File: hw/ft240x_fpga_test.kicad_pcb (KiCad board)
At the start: 4 copper layers, 100 x 42.4 mm, 224 parts, among them J1 Ext_Power, J11 PEN_SEL, J2 USB_C_Receptacle_USB2.0, J3 Jtag_Master, J4 JTAG, J5 GPIO2V5, J6 BNC, J7 BNC, J8 BNC, J9 Conn_02x04_Odd_Even, Q1 Si3477, U1 TLV62569DDC, U10 LMH6882, U11 TSV992A, U12 OPA859xDSG, U13 OPA859xDSG, U14 MCP47CVB02-E_UN, U15 UTC2000, U16 74LVC1G32, U2 TLV62569DDC, U3 TLV62569DDC, U4 FT240XS, U5 XC3S50A-VQ100, U6 AT25DF041B, U7 5P49V5925, U8 THS4522, U9 MAX19507, Y1 25MHz

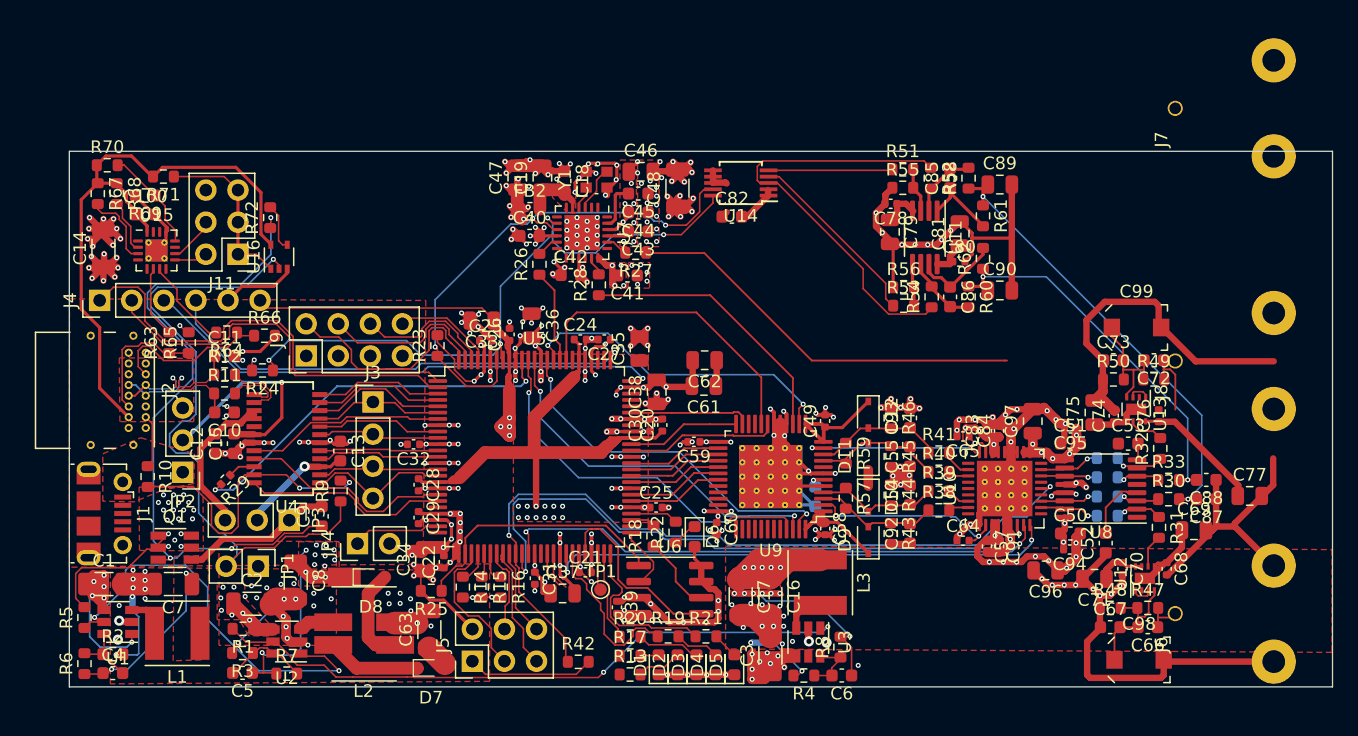
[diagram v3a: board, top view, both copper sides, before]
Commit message: everything hooked up + layed out; 0.2/0.4mm vias :-(
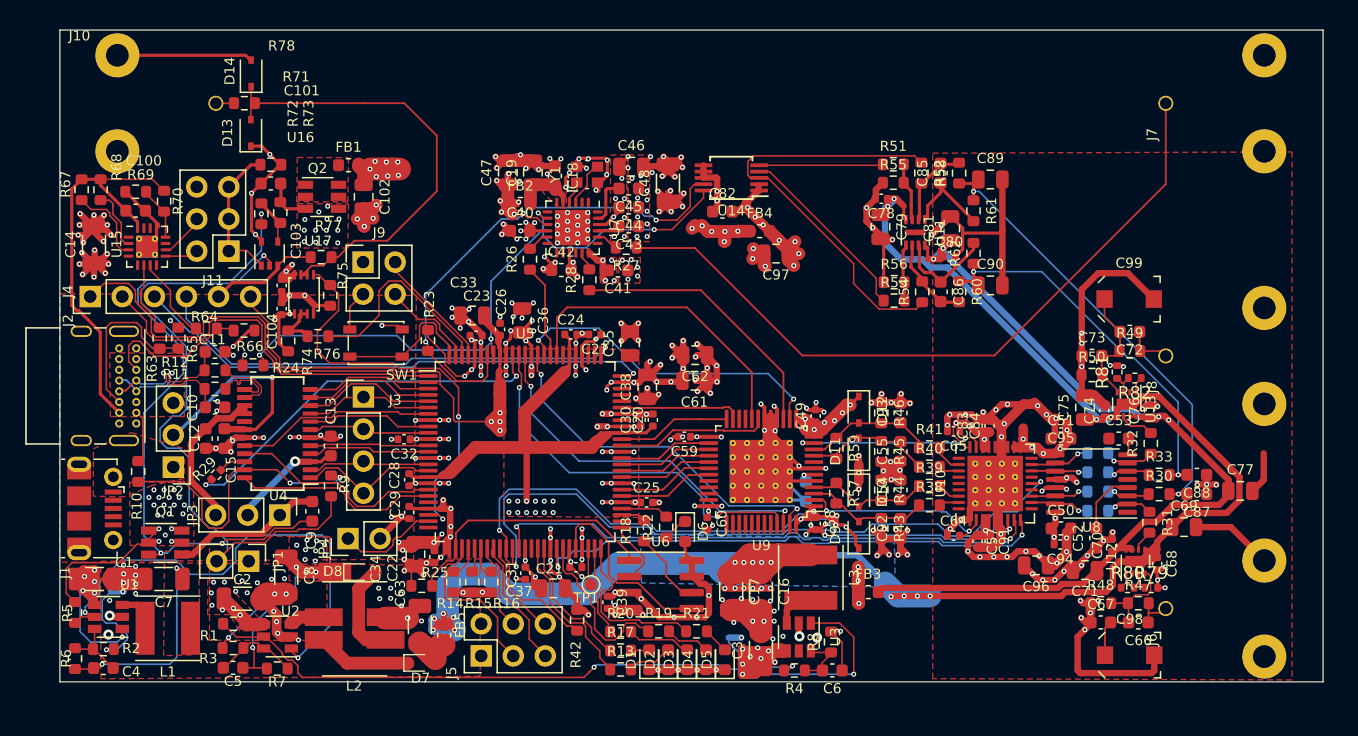
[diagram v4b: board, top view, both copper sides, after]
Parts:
- added C101: 100n, Capacitor_SMD:C_0603_1608Metric, F.Cu at (79.7, 39.4)
- added C102: 1u, Capacitor_SMD:C_0805_2012Metric, F.Cu at (87.0, 40.4)
- added C103: 100n, Capacitor_SMD:C_0402_1005Metric, F.Cu at (80.6, 47.4)
- added C104: 100n, Capacitor_SMD:C_0402_1005Metric, F.Cu at (80.6, 49.3)
- added D13: NSR0170HT1G, Diode_SMD:D_SOD-323, F.Cu at (78.1, 35.3)
- added D14: NSR0170HT1G, Diode_SMD:D_SOD-323, F.Cu at (78.1, 30.6)
- added FB1: Ferrite_Bead MPZ1608S221A, Inductor_SMD:L_0603_1608Metric, F.Cu at (85.8, 37.9)
- added FB3: Ferrite_Bead MPZ1608S221A, Inductor_SMD:L_0603_1608Metric, F.Cu at (127.0, 71.7)
- added FB4: Ferrite_Bead MPZ1608S221A, Inductor_SMD:L_0603_1608Metric, F.Cu at (118.4, 43.1)
- added FB5: Ferrite_Bead MPZ1608S221A, Inductor_SMD:L_0603_1608Metric, F.Cu at (93.4, 75.1)
- added J10: BNC, proj_footprints:BNC_Molex_0731713150, F.Cu at (67.5, 33.0)
- added Q2: Si3477, Package_TO_SOT_SMD:TSOT-23-6, F.Cu at (83.8, 40.4)
- added R73: 100k, Resistor_SMD:R_0603_1608Metric, F.Cu at (80.5, 41.6)
- added R74: 100k, Resistor_SMD:R_0603_1608Metric, F.Cu at (81.1, 51.8)
- added R75: 2k2, Resistor_SMD:R_0603_1608Metric, F.Cu at (84.4, 48.2)
- added R76: 100, Resistor_SMD:R_0603_1608Metric, F.Cu at (83.4, 51.4)
- added R77: 100k, Resistor_SMD:R_0603_1608Metric, F.Cu at (83.7, 45.2)
- added R78: 50, Resistor_SMD:R_0603_1608Metric, F.Cu at (77.6, 33.0)
- added R79: 750, Resistor_SMD:R_0402_1005Metric, F.Cu at (149.4, 71.3)
- added R80: 750, Resistor_SMD:R_0402_1005Metric, F.Cu at (147.5, 71.3)
- added R81: 750, Resistor_SMD:R_0402_1005Metric, F.Cu at (146.7, 54.3)
- added R82: 750, Resistor_SMD:R_0402_1005Metric, F.Cu at (148.1, 54.8)
- added SW1: PROG_B, Button_Switch_SMD:SW_SPST_PTS810, F.Cu at (88.0, 52.0)
- added U17: SN74LVC2T45DCUR, Package_SO:VSSOP-8_2.4x2.1mm_P0.5mm, F.Cu at (82.3, 48.1)
- C67, C73: value 10p -> 15p
- J9: value Conn_02x04_Odd_Even -> PUDC/IN; footprint Connector_PinHeader_2.54mm:PinHeader_2x04_P2.54mm_Vertical -> Connector_PinHeader_2.54mm:PinHeader_2x02_P2.54mm_Vertical
- R38, R39, R40, R41: value 176 -> 178
- U11: footprint Package_SO:MSOP-8_3x3mm_P0.65mm -> proj_footprints:DFN-8-1EP_2x2mm_P0.5mm_EP0.45x1.6mm
- moved C97 24.3 mm to (119.7, 44.9), turned to 180 degrees
- moved J9 8.69 mm to (87.0, 45.6), turned to 0 degrees
- moved R71 8.55 mm to (79.7, 37.9), turned to 0 degrees
- moved R70 5.33 mm to (71.2, 40.8), turned to 270 degrees
- moved R42 3.29 mm to (104.0, 73.9), turned to 90 degrees
- moved C72 2.94 mm to (147.7, 51.1)
- moved R49 2.94 mm to (147.7, 52.6)
- moved C99 2.32 mm to (147.7, 48.5)
- moved C70 2.02 mm to (146.3, 68.0), turned to 90 degrees
- moved NT3 1.84 mm to (116.5, 75.3), turned to 0 degrees
- moved C73 1.74 mm to (144.7, 53.0)
- moved R50 1.74 mm to (144.7, 54.5)
- moved R66 1.67 mm to (77.6, 51.0)
- moved R64 1.63 mm to (74.6, 50.8)
- moved U12 1.53 mm to (148.1, 69.3)
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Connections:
- net Net-(J7-Pad1) renamed /pll_clock/CLK_OUT
- net Net-(R72-Pad2) renamed /Power/PWR_EN
- C49 pad 2: GNDA -> GND
- C50 pad 1: GNDA -> GND
- C51 pad 1: GNDA -> GND
- C52 pad 1: GNDA -> GND
- C53 pad 1: GNDA -> GND
- C57 pad 2: GNDA -> GND
- C58 pad 2: GNDA -> GND
- C63 pad 1: -2V5 -> Net-(C63-Pad1)
- C64 pad 1: GNDA -> GND
- C65 pad 2: GNDA -> GND
- C67 pad 1: GNDA -> GND
- C68 pad 2: GNDA -> GND
- C69 pad 2: GNDA -> GND
- C70 pad 2: GNDA -> GND
- C71 pad 2: GNDA -> GND
- C73 pad 1: GNDA -> GND
- C74 pad 2: GNDA -> GND
- C75 pad 2: GNDA -> GND
- C76 pad 2: GNDA -> GND
- C77 pad 2: GNDA -> GND
- C78 pad 2: GNDA -> GND
- C79 pad 2: GNDA -> GND
- C80 pad 2: GNDA -> GND
- C81 pad 2: GNDA -> GND
- C82 pad 1: GNDA -> GND
- C83 pad 2: GNDA -> GND
- C84 pad 2: GNDA -> GND
- C87 pad 1: GNDA -> GND
- C88 pad 1: GNDA -> GND
- C89 pad 2: GNDA -> GND
- C90 pad 2: GNDA -> GND
- C91 pad 2: GNDA -> GND
- C94 pad 2: GNDA -> GND
- C95 pad 2: GNDA -> GND
- C96 pad 2: GNDA -> GND
- C97 pad 1: Vpp_analog -> +1V8_analog
- C97 pad 2: GNDA -> GND
- C98 pad 2: GNDA -> GND
- C99 pad 2: GNDA -> GND
- D7 pad 2: -2V5 -> Net-(C63-Pad1)
- J6 pad 2: GNDA -> GND
- J8 pad 2: GNDA -> GND
- R48 pad 1: GNDA -> GND
- R50 pad 1: GNDA -> GND
- R55 pad 1: GNDA -> GND
- R56 pad 1: GNDA -> GND
- R71 pad 2: VBUS -> +5V
- U10 pad 1: GNDA -> GND
- U10 pad 21: GNDA -> GND
- U10 pad 22: GNDA -> GND
- U10 pad 23: GNDA -> GND
- U10 pad 37: GNDA -> GND
- U10 pad 5: GNDA -> GND
- U10 pad 6: GNDA -> GND
- U12 pad 1: Net-(U12-Pad1) -> Net-(R80-Pad1)
- U12 pad 3: Net-(U12-Pad1) -> Net-(R79-Pad1)
- U13 pad 1: Net-(U13-Pad1) -> Net-(R82-Pad1)
- U13 pad 3: Net-(U13-Pad1) -> Net-(R81-Pad1)
- U14 pad 6: GNDA -> GND
- U14 pad 7: GNDA -> GND
- U14 pad 8: GNDA -> GND
- U16 pad 5: VBUS -> +5V
- U5 pad 100: Net-(J9-Pad2) -> Net-(SW1-Pad1)
- U5 pad 23: GND -> /fpga_xc3s/IO_DIR
- U5 pad 97: Net-(J9-Pad8) -> Net-(J9-Pad2)
- U5 pad 98: Net-(J9-Pad6) -> /fpga_xc3s/IO_DAT
- U8 pad 12: GNDA -> GND
- U8 pad 16: GNDA -> GND
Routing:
- net GND: track 236.2 -> 419.1 mm, vias 225 -> 304
- net GNDA: track 161.6 -> 0.00 mm, vias 40 -> 0
- net -2V5: track 16.6 -> 156.3 mm, vias 0 -> 13
- net +2V5_analog: track 17.6 -> 75.4 mm, vias 0 -> 4
- net Net-(D13-Pad2): track 0.00 -> 36.6 mm
- net /fpga_xc3s/IO_DIR: track 0.00 -> 33.0 mm, vias 0 -> 2
- net /pll_clock/CLK_OUT: track 31.9 -> 57.2 mm
- net +2V5: track 100.7 -> 125.6 mm, vias 38 -> 39
- net +1V8_analog: track 23.6 -> 44.5 mm, vias 0 -> 22
- net +1V8: track 83.7 -> 103.1 mm, vias 76 -> 92
- net /fpga_xc3s/IO_DAT: track 0.00 -> 16.6 mm
- net VBUS: track 52.4 -> 37.1 mm
- net +5V: track 81.3 -> 95.5 mm, vias 32 -> 49
- net Net-(SW1-Pad1): track 0.00 -> 11.6 mm
- net Net-(J9-Pad6): track 11.2 -> 0.00 mm
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- added copper zone on In2.Cu, net +1V8_analog
- added copper zone on B.Cu, net -2V5
- added copper zone on F.Cu, net Net-(FB1-Pad1)
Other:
- board size 100 x 42.4 mm -> 100 x 51.6 mm
- net class 50OhmLine added: clearance 0.5, trace_width 0.147, via_dia 0.4, via_drill 0.2

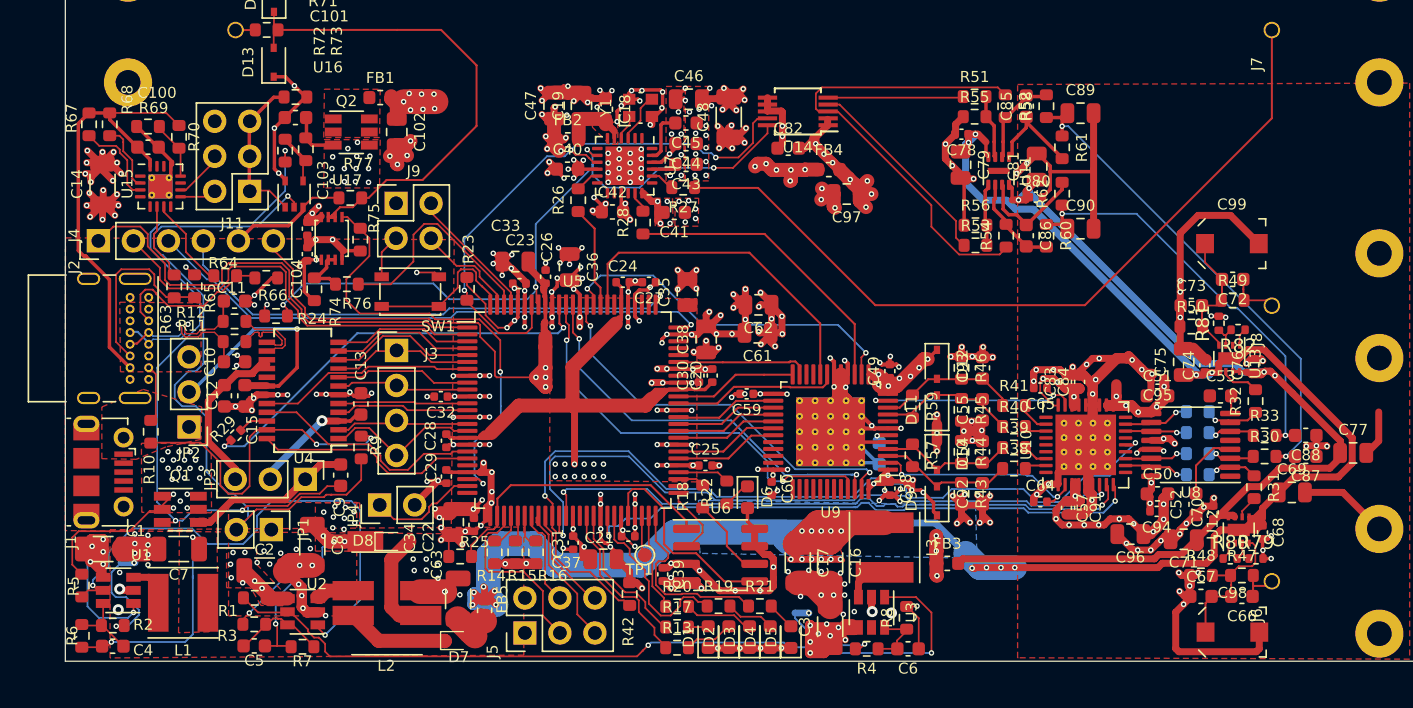
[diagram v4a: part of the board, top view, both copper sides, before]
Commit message: pcb: increased min. via dia to 0.45mm (jlcpcb)
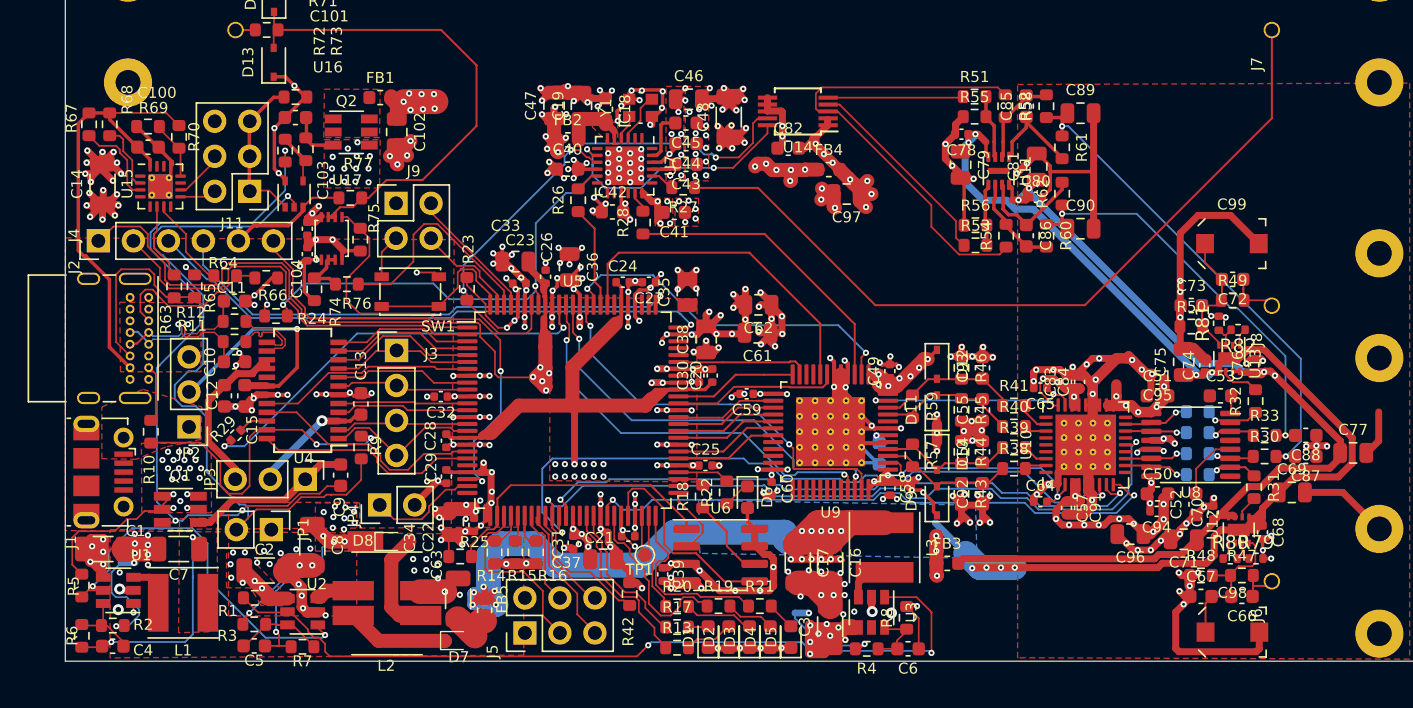
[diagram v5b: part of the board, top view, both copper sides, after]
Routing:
- net -2V5: track 156.3 -> 136.2 mm
- net Net-(R5-Pad1): track 39.3 -> 28.7 mm
- net +5V: track 95.5 -> 88.4 mm
- net GND: track 419.1 -> 422.0 mm, vias 304 -> 307
- net +1V2: track 83.3 -> 85.9 mm, vias 26 -> 27
- net PGA_SDO: track 64.0 -> 61.5 mm
- net +1V8: track 103.1 -> 105.0 mm, vias 92 -> 94
- net PGA_SCLK: track 44.0 -> 45.6 mm
- net +1V8_analog: track 44.5 -> 43.1 mm
- net PGA_CSb: track 41.7 -> 42.9 mm
- net PGA_SDI: track 50.4 -> 51.3 mm
- net Net-(C64-Pad2): track 15.8 -> 16.7 mm
- net ADC_SDIO: track 30.8 -> 30.1 mm
- net +2V5: track 125.6 -> 126.1 mm, vias 39 -> 40
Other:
- net class 50OhmLine: via_dia 0.4 -> 0.45
- net class Default: via_dia 0.4 -> 0.45
- net class clr3p5: via_dia 0.4 -> 0.45
- rule via_min_size: 0.4 -> 0.45

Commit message: prototype version
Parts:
- added D15: LED_Front, proj_footprints:LED_Wuerth_Sideview, F.Cu at (65.6, 41.5)
- added J12: PUDC_B/IN, Connector_PinHeader_2.54mm:PinHeader_2x02_P2.54mm_Vertical, F.Cu at (89.5, 48.3)
- added R83: 1k5, Resistor_SMD:R_0603_1608Metric, F.Cu at (64.8, 38.6)
- added R84: 1k5, Resistor_SMD:R_0603_1608Metric, F.Cu at (66.8, 41.0)
- added TP2: Ref, proj_footprints:TestPoint_Pad_D0.8mm_no_CY, F.Cu at (105.6, 40.8)
- J9: value PUDC/IN -> Expansion; footprint Connector_PinHeader_2.54mm:PinHeader_2x02_P2.54mm_Vertical -> Connector_PinHeader_2.54mm:PinHeader_2x04_P2.54mm_Vertical
- R79, R81: value 750 -> 150
- moved J9 58.2 mm to (136.2, 76.6), turned to 270 degrees
- moved C14 18.8 mm to (82.6, 35.9), turned to 0 degrees
- moved R67 6.10 mm to (66.3, 45.7), turned to 0 degrees
- moved R68 4.39 mm to (66.3, 44.2), turned to 0 degrees
- moved R69 2.37 mm to (71.2, 40.8), turned to 90 degrees
- moved R70 2.34 mm to (69.0, 40.0), turned to 0 degrees
- moved J1 0.28 mm to (65.5, 65.1)
- moved J6 0.25 mm to (158.6, 73.0)
- moved J7 0.25 mm to (158.6, 33.0)
- moved J8 0.25 mm to (158.6, 53.0)
- moved J10 0.15 mm to (67.4, 33.0)
- moved C27 0.05 mm to (105.3, 51.2)
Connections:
- net Net-(D13-Pad2) renamed /fpga_xc3s/sheet60F7998F/DIGIO
- C63 pad 1: Net-(C63-Pad1) -> /Power/-2V5_dig
- D7 pad 2: Net-(C63-Pad1) -> /Power/-2V5_dig
- FB5 pad 1: Net-(C63-Pad1) -> /Power/-2V5_dig
- J9 pad 2: Net-(J9-Pad2) -> /Power/-2V5_dig
- J9 pad 3: GND -> EXP_IO1_1V8
- J9 pad 4: Net-(J9-Pad4) -> +1V8
- U5 pad 23: /fpga_xc3s/IO_DIR -> GND
- U5 pad 52: Net-(U5-Pad52) -> /fpga_xc3s/LED_FRONT_G
- U5 pad 71: Net-(U5-Pad71) -> /fpga_xc3s/IO_DIR
- U5 pad 72: Net-(U5-Pad71) -> Net-(U5-Pad72)
- U5 pad 73: Net-(U5-Pad73) -> Net-(U5-Pad72)
- U5 pad 77: Net-(U5-Pad77) -> EXP_IO1_1V8
- U5 pad 78: Net-(U5-Pad78) -> EXP_IO2_1V8
- U5 pad 97: Net-(J9-Pad2) -> Net-(J12-Pad3)
- U5 pad 99: Net-(J9-Pad4) -> Net-(J12-Pad1)
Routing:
- net /fpga_xc3s/LED_FRONT_G: track 0.00 -> 73.4 mm, vias 0 -> 2
- net EXP_IO2_1V8: track 0.00 -> 65.2 mm, vias 0 -> 1
- net Net-(R83-Pad1): track 0.00 -> 63.8 mm, vias 0 -> 2
- net -2V5: track 136.2 -> 199.5 mm, vias 13 -> 26
- net EXP_IO1_1V8: track 0.00 -> 61.6 mm, vias 0 -> 1
- net /Power/-2V5_dig: track 0.00 -> 48.7 mm
- net +2V5_analog: track 75.4 -> 113.4 mm, vias 4 -> 15
- net +2V5: track 126.1 -> 162.5 mm, vias 40 -> 46
- net +1V8: track 105.0 -> 138.6 mm
- net +5V: track 88.4 -> 102.4 mm
- net Net-(J9-Pad2): track 9.90 -> 0.00 mm
- net Net-(J12-Pad3): track 0.00 -> 9.53 mm
- net VBUS: track 37.1 -> 28.1 mm
- net PGA_SDI: track 51.3 -> 59.4 mm
- net Net-(J12-Pad1): track 0.00 -> 7.74 mm
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- added copper zone on In2.Cu, net GND
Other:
- board size 100 x 51.6 mm -> 100 x 60 mm
- rule trace_min: 0 -> 0.1
- board text added: "USBFastADC V1.0.0"
